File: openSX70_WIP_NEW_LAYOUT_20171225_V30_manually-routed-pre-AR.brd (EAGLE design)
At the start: 95.9 x 27.9 mm, 37 parts, among them Q1 5.8A/30V/35mΩ, Q2 5.8A/30V/35mΩ, U1 ATMEGA328P_TQFP, U3 BH1750FVI-TR, Y1 CSTCE16M0V53-R0

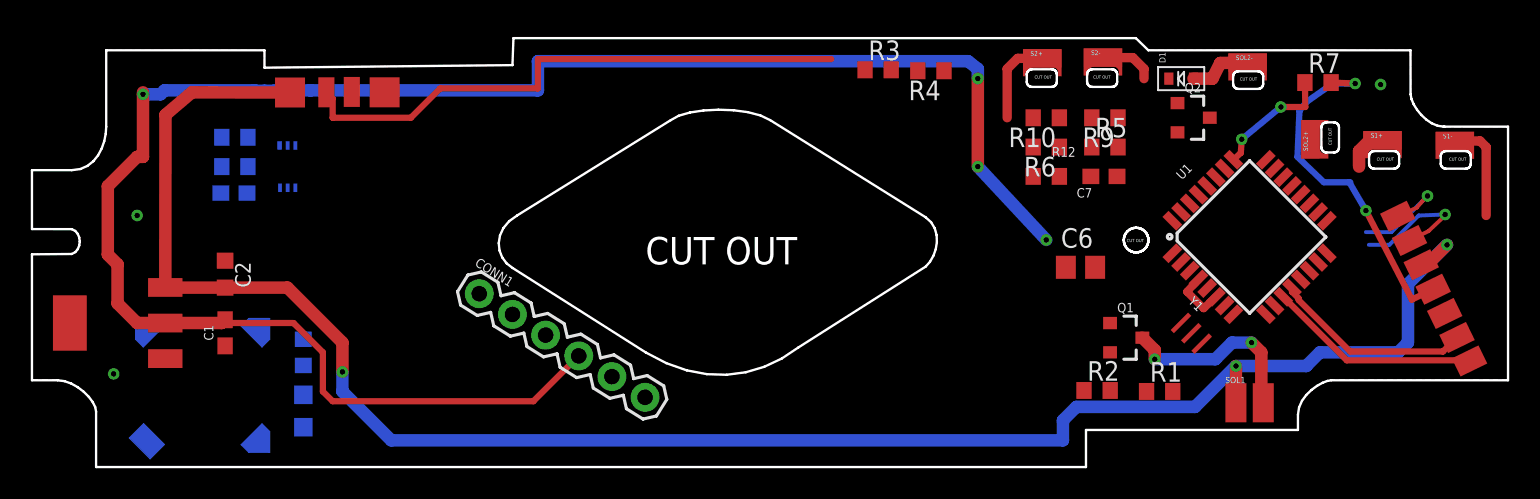
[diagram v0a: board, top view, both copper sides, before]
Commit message: fixed connections on openSX70 library
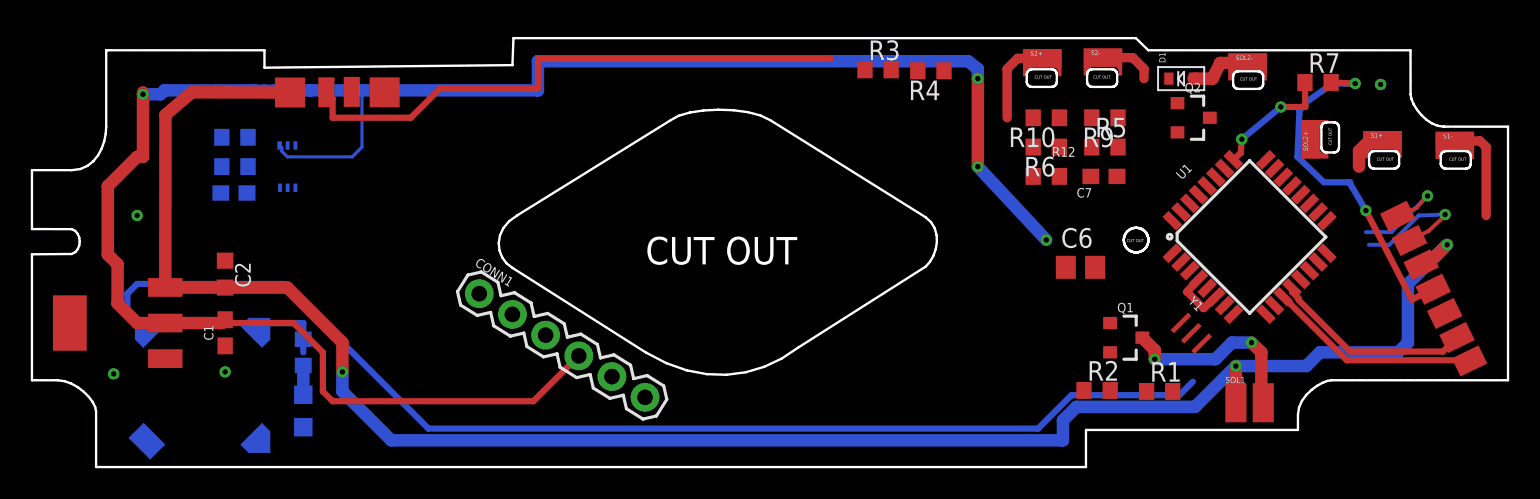
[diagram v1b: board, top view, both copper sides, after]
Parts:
- turned R8 to 270 degrees
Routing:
- net BUZZER: track 0.00 -> 79.4 mm
- net 3.3V: track 127.4 -> 137.2 mm
- net N$26: track 0.00 -> 5.34 mm
- net N$5: track 0.00 -> 1.91 mm
- net GND: vias 3 -> 4
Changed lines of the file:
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@@
 <?xml version="1.0" encoding="utf-8"?>
 <!DOCTYPE eagle SYSTEM "eagle.dtd">
-<eagle version="8.4.3">
+<eagle version="8.5.1">
 <drawing>
 <settings>
@@
 <grid distance="25" unitdist="mil" unit="mil" style="lines" multiple="1" display="no" altdistance="2.5" altunitdist="mil" altunit="mil"/>
 <layers>
-<layer number="1" name="Top" color="4" fill="1" visible="yes" active="yes"/>
+<layer number="1" name="Top" color="4" fill="1" visible="no" active="yes"/>
 <layer number="16" name="Bottom" color="1" fill="1" visible="yes" active="yes"/>
 <layer number="17" name="Pads" color="2" fill="1" visible="yes" active="yes"/>
@@
 <param name="checkRestrict" value="1"/>
 <param name="checkStop" value="0"/>
+<param name="checkValues" value="0"/>
 <param name="useDiameter" value="13"/>
 <param name="maxErrors" value="50"/>
@@
 <attribute name="PROD_ID" value="CAP-11015" x="14.605" y="9.525" size="1.778" layer="27" rot="R90" display="off"/>
 </element>
-<element name="C2" library="rcl" library_urn="urn:adsk.eagle:library:334" package="C0603K" package3d_urn="urn:adsk.eagle:package:23680/2" value="100nF" x="14.605" y="13.335" rot="R270"/>
+<element name="C2" library="rcl" library_urn="urn:adsk.eagle:library:334" package="C0603K" package3d_urn="urn:adsk.eagle:package:23680/2" value="100nF" x="14.605" y="13.335" rot="R270">
+<attribute name="SPICEPREFIX" value="C" x="14.605" y="13.335" size="1.778" layer="27" rot="R270" display="off"/>
+</element>
 <element name="C5" library="SparkFun-Capacitors" package="0603" value="10uF" x="15.1765" y="18.6055" rot="MR0">
 <attribute name="PROD_ID" value="CAP-11015" x="15.1765" y="18.6055" size="1.778" layer="28" rot="MR0" display="off"/>
@@
 <attribute name="PRICE" value="None" x="7.62" y="10.16" size="1.778" layer="27" rot="R180" display="off"/>
 </element>
-<element name="LED1" library="led" library_urn="urn:adsk.eagle:library:259" package="CHIPLED_0805" package3d_urn="urn:adsk.eagle:package:15821/1" value="" x="19.685" y="4.445" rot="MR0"/>
+<element name="LED1" library="led" library_urn="urn:adsk.eagle:library:259" package="CHIPLED_0805" package3d_urn="urn:adsk.eagle:package:15821/2" value="" x="19.685" y="4.445" rot="MR0"/>
 <element name="Q1" library="openSX70" package="SOT23-3" value="5.8A/30V/35mΩ" x="73.0885" y="9.2075" rot="R270">
 <attribute name="PROD_ID" value="TRANS-12988" x="73.0885" y="9.2075" size="1.778" layer="27" rot="R270" display="off"/>
@@
 <element name="R6" library="resistor" library_urn="urn:adsk.eagle:library:348" package="R0603" package3d_urn="urn:adsk.eagle:package:26057/1" value="15K" x="67.945" y="21.59" rot="R180"/>
 <element name="R7" library="resistor" library_urn="urn:adsk.eagle:library:348" package="R0603" package3d_urn="urn:adsk.eagle:package:26057/1" value="100R" x="85.598" y="25.781"/>
-<element name="R8" library="resistor" library_urn="urn:adsk.eagle:library:348" package="R0603" package3d_urn="urn:adsk.eagle:package:26057/1" value="470R" x="19.685" y="8.255" rot="MR90"/>
+<element name="R8" library="resistor" library_urn="urn:adsk.eagle:library:348" package="R0603" package3d_urn="urn:adsk.eagle:package:26057/1" value="470R" x="19.685" y="8.255" rot="MR270"/>
 <element name="R9" library="resistor" library_urn="urn:adsk.eagle:library:348" package="R0603" package3d_urn="urn:adsk.eagle:package:26057/1" value="12K" x="71.755" y="23.495" rot="R180"/>
 <element name="S1+" library="openSX70" package="SX70-S-PAD" value="SX70_S-PAD" x="89.779" y="21.945"/>
@@
 <contactref element="U1" pad="10"/>
 <contactref element="BUZZ1" pad="+"/>
-<wire x1="9.7127" y1="9.5306" x2="82.7741125" y2="11.298459375" width="0" layer="19" extent="1-16"/>
+<wire x1="9.7127" y1="9.5306" x2="9.02438125" y2="10.21891875" width="0.1524" layer="16"/>
+<wire x1="9.02433125" y1="9.5306" x2="9.7127" y2="9.5306" width="0.1524" layer="16"/>
+<wire x1="9.7127" y1="9.5306" x2="8.255" y2="10.9883" width="0.4064" layer="16"/>
+<wire x1="8.255" y1="10.9883" x2="8.255" y2="12.065" width="0.4064" layer="16"/>
+<wire x1="8.255" y1="12.065" x2="8.89" y2="12.7" width="0.4064" layer="16"/>
+<wire x1="8.89" y1="12.7" x2="18.415" y2="12.7" width="0.4064" layer="16"/>
+<wire x1="18.415" y1="12.7" x2="27.813" y2="3.302" width="0.4064" layer="16"/>
+<wire x1="76.5943" y1="5.4743" x2="77.47" y2="6.35" width="0.4064" layer="16"/>
+<wire x1="69.589525" y1="5.4743" x2="76.5943" y2="5.4743" width="0.4064" layer="16"/>
+<wire x1="67.417225" y1="3.302" x2="69.589525" y2="5.4743" width="0.4064" layer="16"/>
+<wire x1="27.813" y1="3.302" x2="67.417225" y2="3.302" width="0.4064" layer="16"/>
+<wire x1="77.47" y1="6.35" x2="82.7741125" y2="11.298459375" width="0" layer="19" extent="1-16"/>
 </signal>
 <signal name="S2">
@@
 <wire x1="16.556278125" y1="25.24240625" x2="17.169203125" y2="25.2487" width="0.8128" layer="16"/>
 <wire x1="17.169203125" y1="25.2487" x2="17.78234375" y2="25.2487" width="0.8128" layer="16"/>
-<wire x1="17.78234375" y1="25.2487" x2="20.148978125" y2="25.273" width="0.8128" layer="16"/>
-<wire x1="20.148978125" y1="25.273" x2="34.925" y2="25.273" width="0.8128" layer="16"/>
+<wire x1="17.78234375" y1="25.2487" x2="19.0449" y2="25.2616625" width="0.8128" layer="16"/>
+<wire x1="19.0449" y1="25.2616625" x2="20.148978125" y2="25.273" width="0.8128" layer="16"/>
+<wire x1="20.148978125" y1="25.273" x2="23.495" y2="25.273" width="0.8128" layer="16"/>
+<wire x1="23.495" y1="25.273" x2="34.925" y2="25.273" width="0.8128" layer="16"/>
 <wire x1="78.9662" y1="11.86414375" x2="78.1685" y2="11.1125" width="0.508" layer="1"/>
 <wire x1="78.1685" y1="11.1125" x2="77.089" y2="12.192" width="0.508" layer="1"/>
@@
 <wire x1="19.05" y1="10.16" x2="20.955" y2="8.255" width="0.4064" layer="1"/>
 <wire x1="21.59" y1="5.08" x2="34.6301125" y2="5.08" width="0.4064" layer="1"/>
+<wire x1="18.144" y1="21.695" x2="18.29" y2="21.549" width="0.2032" layer="16"/>
+<wire x1="18.29" y1="21.549" x2="18.29" y2="21.3147875" width="0.2032" layer="16"/>
+<wire x1="18.29" y1="21.3147875" x2="18.6497875" y2="20.955" width="0.2032" layer="16"/>
+<wire x1="18.6497875" y1="20.955" x2="22.86" y2="20.955" width="0.2032" layer="16"/>
+<wire x1="22.86" y1="20.955" x2="23.495" y2="21.59" width="0.2032" layer="16"/>
+<wire x1="23.495" y1="21.59" x2="23.495" y2="25.273" width="0.2032" layer="16"/>
 <wire x1="78.9662" y1="11.86414375" x2="85.6025375" y2="17.3691125" width="0" layer="19" extent="1-1"/>
 <wire x1="69.2175" y1="13.7795" x2="77.089" y2="12.192" width="0" layer="19" extent="1-1"/>
 <wire x1="67.945" y1="15.5575" x2="69.2175" y2="13.7795" width="0" layer="19" extent="1-1"/>
-<wire x1="18.144" y1="21.695" x2="17.78234375" y2="25.2487" width="0" layer="19" extent="16-16"/>
 <wire x1="67.095" y1="19.685" x2="63.5" y2="20.32" width="0" layer="19" extent="1-16"/>
 <wire x1="14.39" y1="20.32" x2="18.144" y2="21.695" width="0" layer="19" extent="16-16"/>
@@
 <via x="89.662" y="25.654" extent="1-16" drill="0.35"/>
 <via x="7.366" y="6.858" extent="1-16" drill="0.35"/>
-<wire x1="16.5693" y1="9.5279" x2="14.605" y2="8.675" width="0" layer="19" extent="1-16"/>
+<via x="14.605" y="6.985" extent="1-16" drill="0.35"/>
+<wire x1="14.605" y1="8.675" x2="16.5693" y2="9.5279" width="0" layer="19" extent="1-16"/>
 <wire x1="24.9682" y1="25.146" x2="19.169" y2="21.695" width="0" layer="19" extent="1-16"/>
 </signal>
@@
 <contactref element="R8" pad="2"/>
 <contactref element="LED1" pad="C"/>
-<wire x1="19.685" y1="5.495" x2="19.685" y2="9.105" width="0" layer="19" extent="16-16"/>
+<wire x1="19.685" y1="5.495" x2="19.685" y2="7.405" width="0.8128" layer="16"/>
 </signal>
 <signal name="DTR">
@@
 <wire x1="84.7725" y1="24.1935" x2="84.748" y2="25.781" width="0.4064" layer="1"/>
 </signal>
+<signal name="N$26">
+<wire x1="16.51" y1="9.525" x2="17.145" y2="10.16" width="0.4064" layer="16"/>
+<wire x1="17.145" y1="10.16" x2="19.685" y2="10.16" width="0.4064" layer="16"/>
+<wire x1="19.685" y1="10.16" x2="19.685" y2="8.89" width="0.4064" layer="16"/>
+<wire x1="19.685" y1="8.255" x2="19.685" y2="8.89" width="0.4064" layer="16"/>
+</signal>
 </signals>
